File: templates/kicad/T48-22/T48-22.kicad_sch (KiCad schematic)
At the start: 22 parts

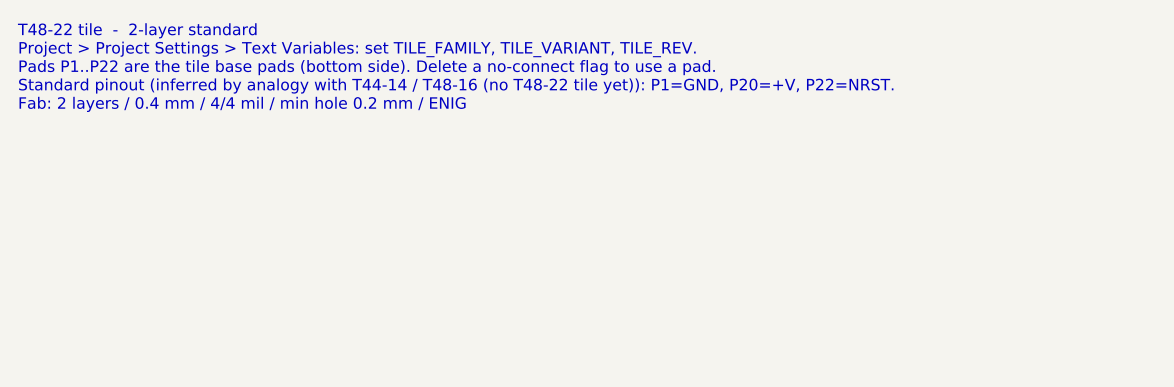
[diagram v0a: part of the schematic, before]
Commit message: Re-tier on measured prices: 4L on 0.2 mm drill, add 4L-fine
4L keeps the 0.2 mm drill so it lands in PCBWay's $162 standard bucket
rather than the $419 one; 3/3 mil and 0.15 mm drills move to a new 4L-fine
tier on the advanced form. Quotes name the calculator to use. set_tier.py
gains --package for projects that predate the templates and --ignore-locks
for stale lock files.

Co-Authored-By: Claude Fable 5.1 <noreply@anthropic.com>
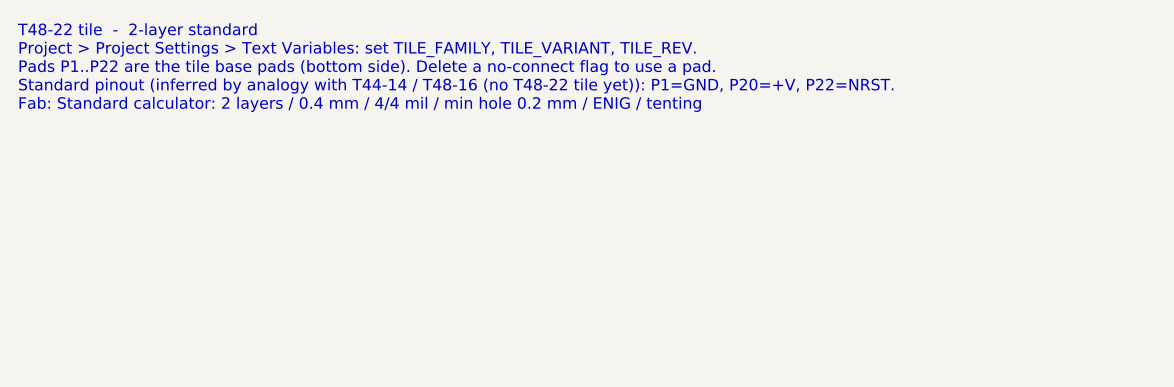
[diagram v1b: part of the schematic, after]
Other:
- note added: "T48-22 tile - 2-layer standard Project > Project Settings > Text Variables: set TILE_FAMILY, TILE_VARIANT, TILE_REV. Pads P1..P22 are the tile base pads (bottom side). Delete a no-connect flag to use a pad. Standard pinout (inferred by analogy with T44-14 / T48-16 (no T48-22 tile yet)): P1=GND, P20=+V, P22=NRST. Fab: Standard calculator: 2 layers / 0.4 mm / 4/4 mil / min hole 0.2 mm / ENIG / tent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"
- note removed: "T48-22 tile - 2-layer standard Project > Project Settings > Text Variables: set TILE_FAMILY, TILE_VARIANT, TILE_REV. Pads P1..P22 are the tile base pads (bottom side). Delete a no-connect flag to use a pad. Standard pinout (inferred by analogy with T44-14 / T48-16 (no T48-22 tile yet)): P1=GND, P20=+V, P22=NRST. Fab: 2 layers / 0.4 mm / 4/4 mil / min hole 0.2 mm / ENIG"
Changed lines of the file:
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@@
 		(comment 2 "${FAB_QUOTE}")
 	)
-	(text "T48-22 tile  -  2-layer standard\nProject > Project Settings > Text Variables: set TILE_FAMILY, TILE_VARIANT, TILE_REV.\nPads P1..P22 are the tile base pads (bottom side). Delete a no-connect flag to use a pad.\nStandard pinout (inferred by analogy with T44-14 / T48-16 (no T48-22 tile yet)): P1=GND, P20=+V, P22=NRST.\nFab: 2 layers / 0.4 mm / 4/4 mil / min hole 0.2 mm / ENIG"
+	(text "T48-22 tile  -  2-layer standard\nProject > Project Settings > Text Variables: set TILE_FAMILY, TILE_VARIANT, TILE_REV.\nPads P1..P22 are the tile base pads (bottom side). Delete a no-connect flag to use a pad.\nStandard pinout (inferred by analogy with T44-14 / T48-16 (no T48-22 tile yet)): P1=GND, P20=+V, P22=NRST.\nFab: Standard calculator: 2 layers / 0.4 mm / 4/4 mil / min hole 0.2 mm / ENIG / tenting"
 		(exclude_from_sim no)
 		(at 25.4 25.4 0)
